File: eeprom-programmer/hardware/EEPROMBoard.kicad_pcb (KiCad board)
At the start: 2 copper layers, 13 parts, among them J1 DB9_Female, U1 MAX232, U2 28C256, U3 ATtiny2313V-10PU, U4 74HC595, U5 74HC595

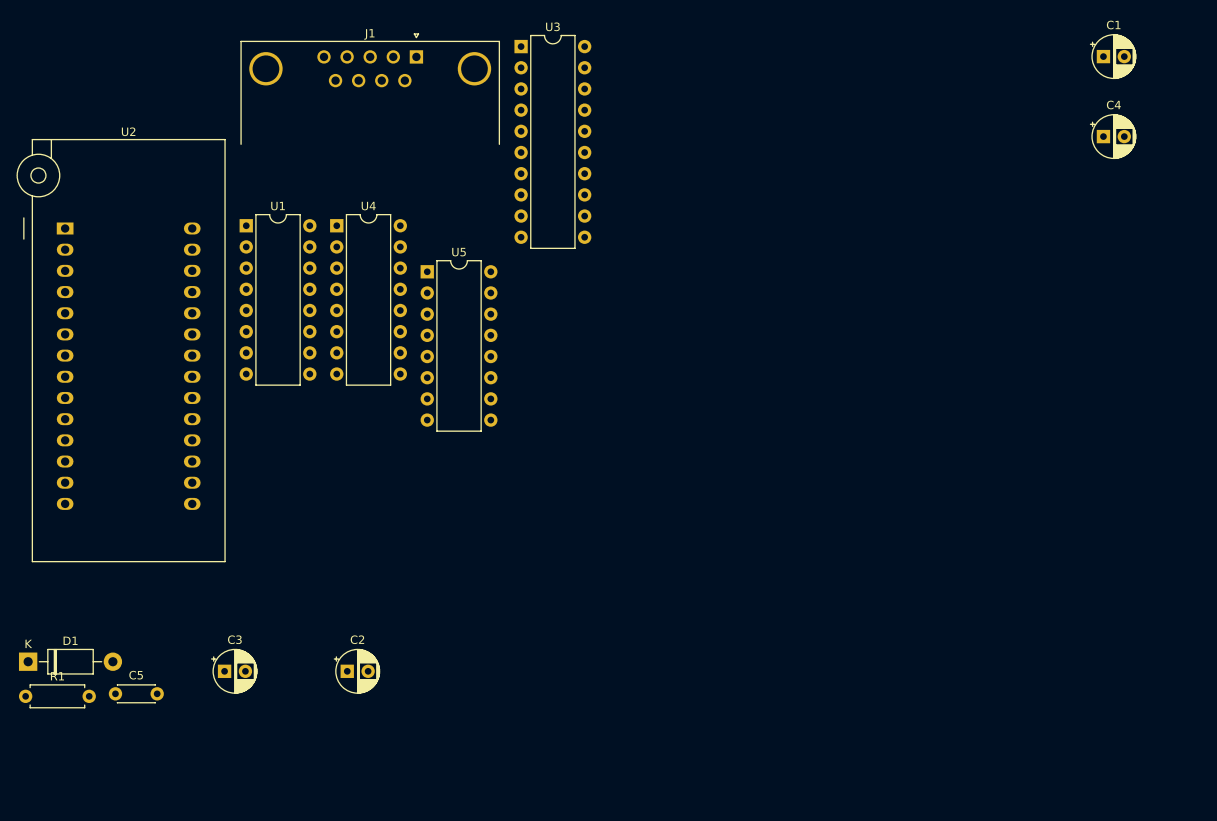
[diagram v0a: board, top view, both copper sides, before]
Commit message: Add some headers to make a 28-pin ZIF socket into a 40 pin one.
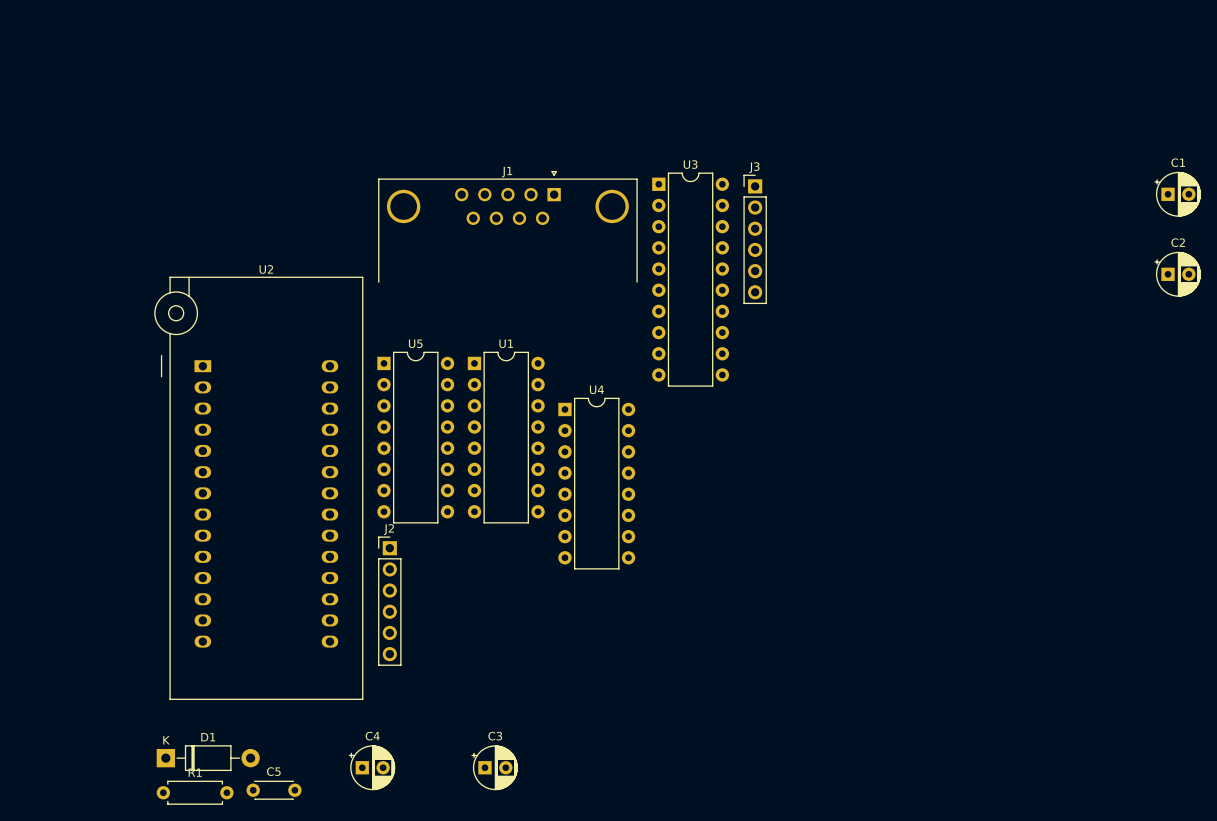
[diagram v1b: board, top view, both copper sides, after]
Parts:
- added J2: Conn_01x06, Connector_PinHeader_2.54mm:PinHeader_1x06_P2.54mm_Vertical, F.Cu at (114.6, 83.3)
- added J3: Conn_01x06, Connector_PinHeader_2.54mm:PinHeader_1x06_P2.54mm_Vertical, F.Cu at (158.4, 39.9)
- moved C4 116.7 mm to (111.3, 109.6)
- moved C2 109.3 mm to (207.9, 50.5)
- moved U4 35.1 mm to (135.6, 66.7)
- moved C3 33.3 mm to (126.0, 109.6)
- moved U1 32.0 mm to (124.7, 61.2)
- moved U3 23.3 mm to (146.8, 39.7)
- moved U2 23.3 mm to (92.2, 61.5)
- moved J1 23.3 mm to (134.3, 40.9)
- moved R1 20.2 mm to (87.4, 112.6)
- moved C5 20.2 mm to (98.2, 112.3)
- moved D1 20.2 mm to (87.7, 108.5)
- moved C1 18.2 mm to (207.9, 40.9)
- moved U5 12.2 mm to (113.9, 61.2)
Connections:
- J1 pad 2: (no net) -> N$32
- J1 pad 3: (no net) -> N$33
- U1 pad 13: (no net) -> N$33
- U1 pad 14: (no net) -> N$32
